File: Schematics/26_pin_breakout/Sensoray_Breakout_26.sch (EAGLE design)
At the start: 14 parts, among them X1 87758-2616

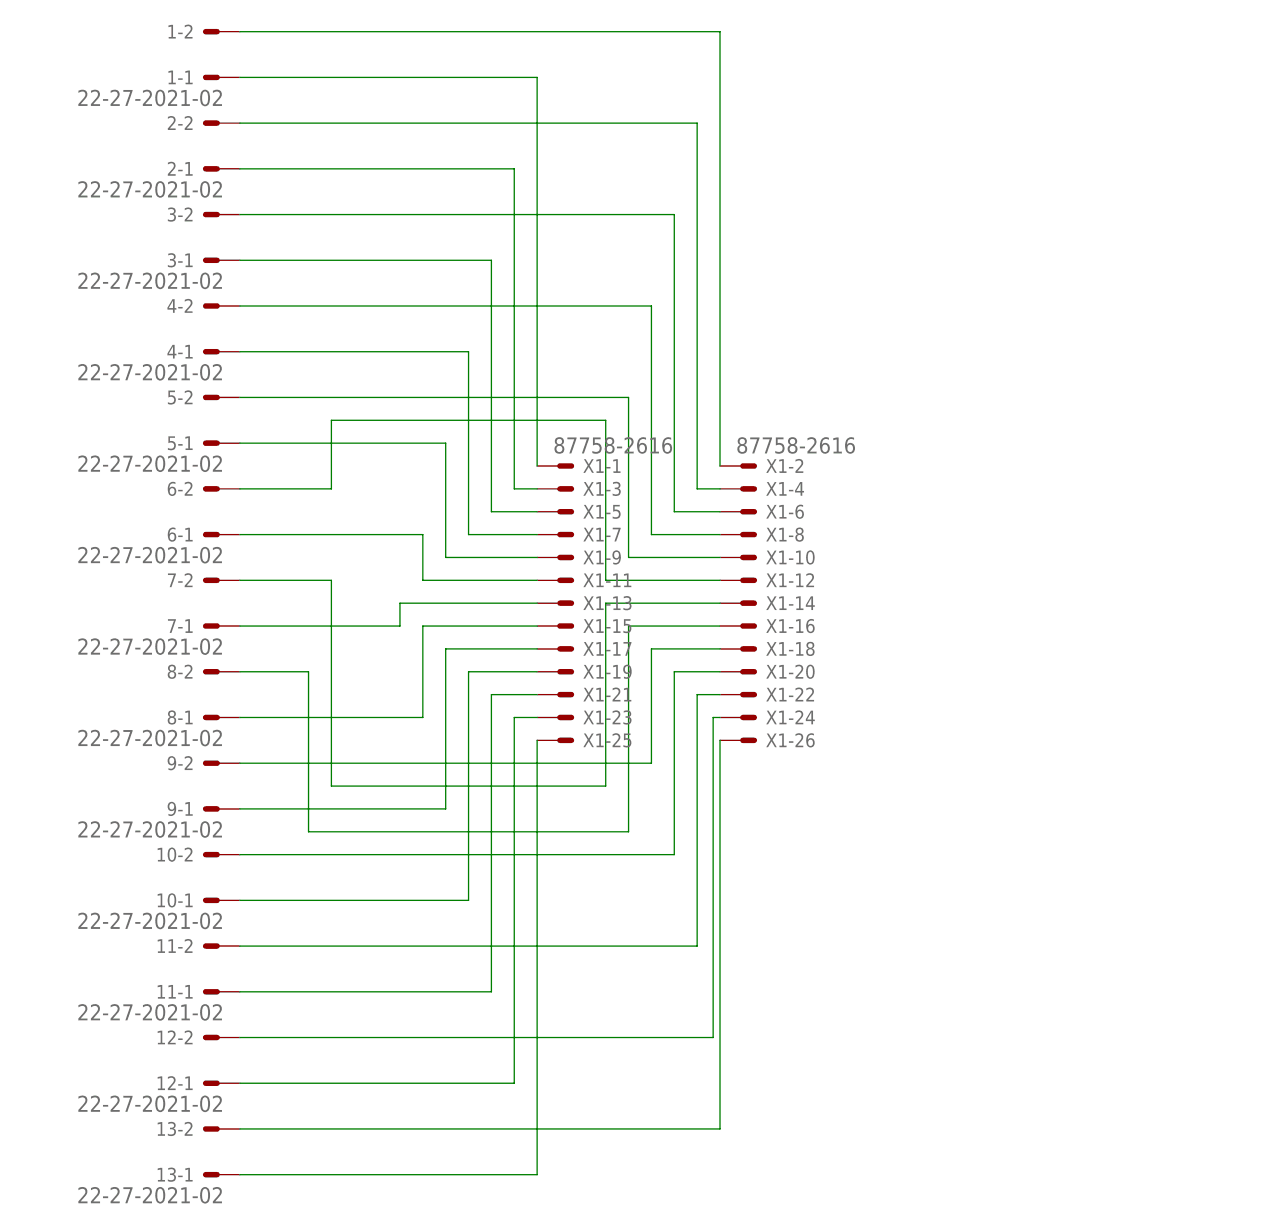
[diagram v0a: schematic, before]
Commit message: added Rev 2 for 26 and 50 pin breakout boards, along with their gerber files for 1-layer PCB use. also added WPR for week of 27th
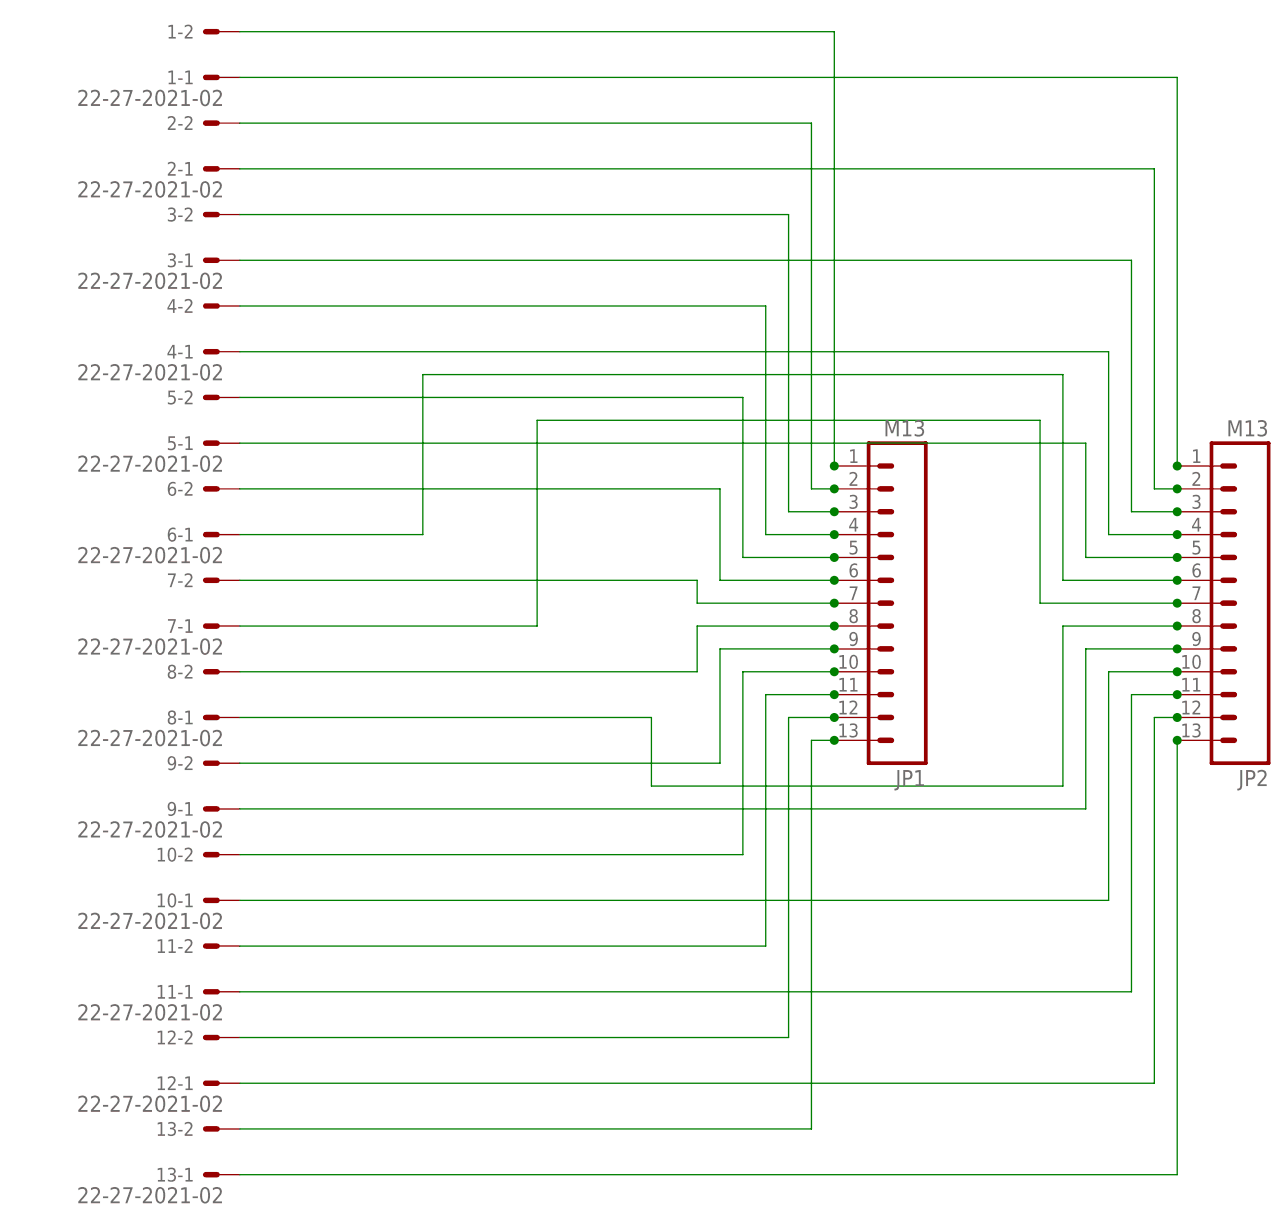
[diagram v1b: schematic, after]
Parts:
- removed X1: 87758-2616, con-molex:87758-2616
- added JP1, JP2: M13, SparkFun-Connectors:M13
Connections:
- net N$1: now also 1-2.S, JP1.1; no longer 1-1.S, X1-1.S
- net N$10: now also 10-2.S, JP1.10; no longer 9-1.S, X1-17.S
- net N$11: now also 11-2.S, JP1.11; no longer 10-1.S, X1-19.S
- net N$12: now also 12-2.S, JP1.12; no longer 11-1.S, X1-21.S
- net N$13: now also 13-2.S, JP1.13; no longer 12-1.S, X1-23.S
- net N$14: now also 1-1.S, JP2.1; no longer 13-1.S, X1-25.S
- net N$15: now also 2-1.S, JP2.2; no longer 2-2.S, X1-4.S
- net N$16: now also 3-1.S, JP2.3; no longer 3-2.S, X1-6.S
- net N$17: now also 4-1.S, JP2.4; no longer 4-2.S, X1-8.S
- net N$18: now also 5-1.S, JP2.5; no longer 5-2.S, X1-10.S
- net N$19: now also 6-1.S, JP2.6; no longer 6-2.S, X1-12.S
- net N$2: now also 2-2.S, JP1.2; no longer 1-2.S, X1-2.S
- net N$20: now also 7-1.S, JP2.7; no longer 7-2.S, X1-14.S
- net N$21: now also 13-1.S, JP2.13; no longer 8-2.S, X1-16.S
- net N$22: now also 12-1.S, JP2.12; no longer 9-2.S, X1-18.S
- net N$23: now also 11-1.S, JP2.11; no longer 10-2.S, X1-20.S
- net N$24: now also 10-1.S, JP2.10; no longer 11-2.S, X1-22.S
- net N$25: now also 9-1.S, JP2.9; no longer 12-2.S, X1-24.S
- net N$26: now also 8-1.S, JP2.8; no longer 13-2.S, X1-26.S
- net N$3: now also 3-2.S, JP1.3; no longer 2-1.S, X1-3.S
- net N$4: now also 4-2.S, JP1.4; no longer 3-1.S, X1-5.S
- net N$5: now also 5-2.S, JP1.5; no longer 4-1.S, X1-7.S
- net N$6: now also 6-2.S, JP1.6; no longer 5-1.S, X1-9.S
- net N$7: now also 7-2.S, JP1.7; no longer 6-1.S, X1-11.S
- net N$8: now also 8-2.S, JP1.8; no longer 7-1.S, X1-13.S
- net N$9: now also 9-2.S, JP1.9; no longer 8-1.S, X1-15.S
